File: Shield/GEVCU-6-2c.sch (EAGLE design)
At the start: 242 parts, among them IC10 ISO1050DW, IC9 ISO1050DW, U1 ATSAM3X8EA-AU, U11 ADE7913, U12 ADE7913, U24 ADE7913, U3 ADUM3221BRZ, U4 ADUM3221BRZ, U5 ADUM3221BRZ, U6 ADUM3221BRZ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

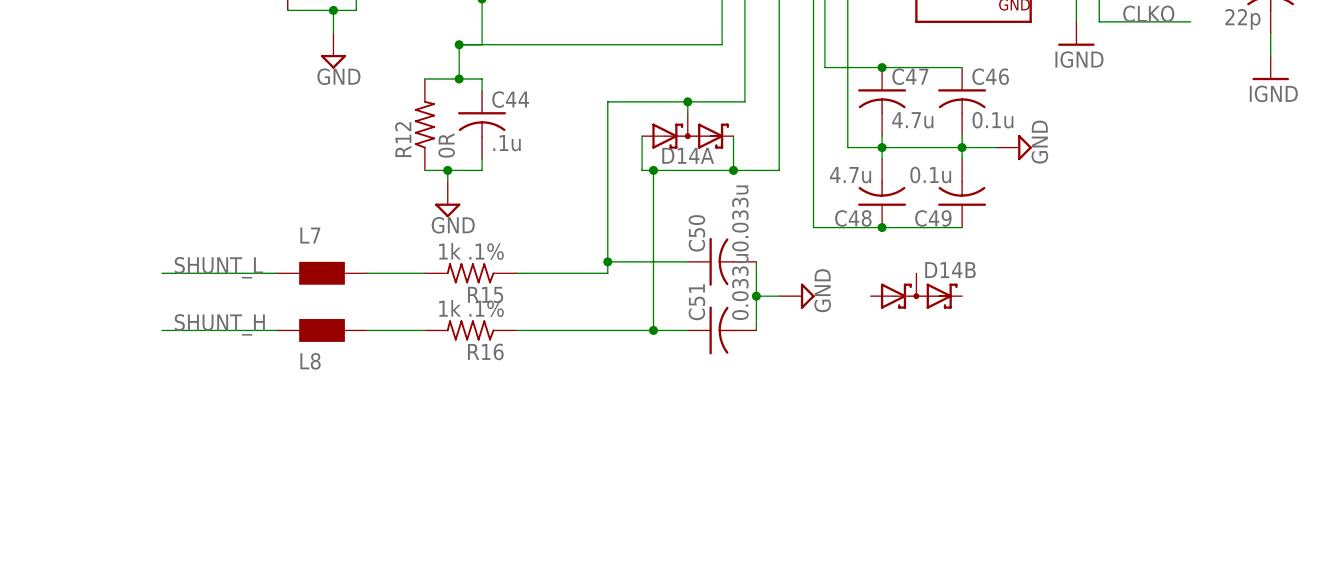
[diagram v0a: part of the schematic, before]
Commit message: Fixes on GEVCU board files, addition of an Eagle library that contains some of the parts on the GEVCU board.
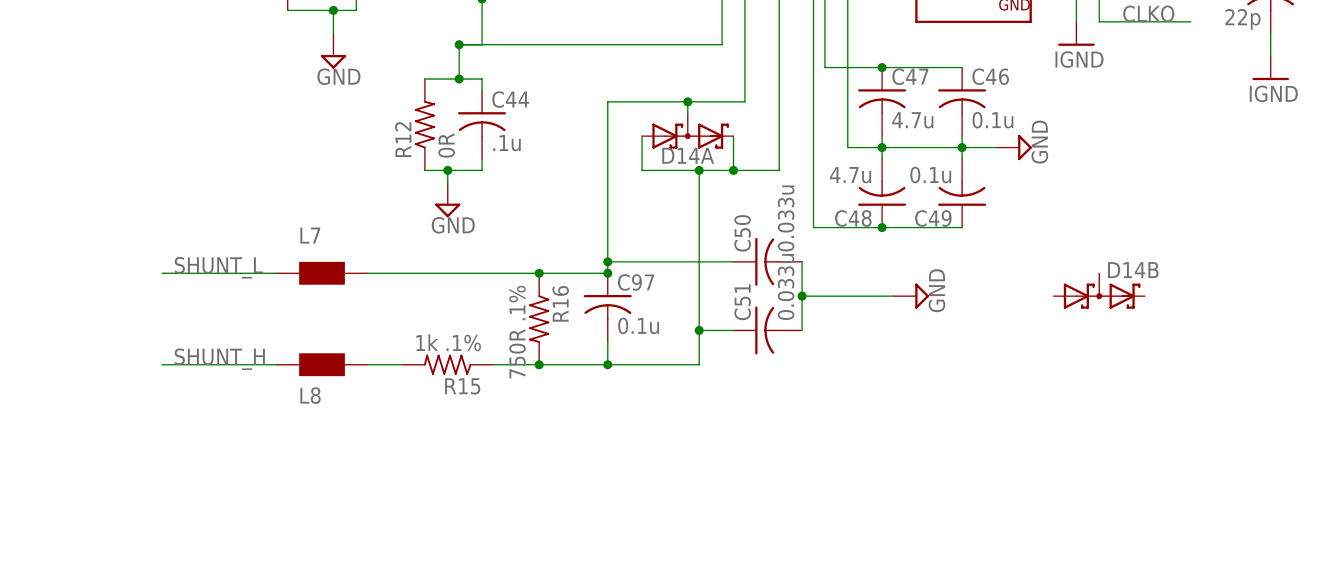
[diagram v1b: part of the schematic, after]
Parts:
- added C97: 0.1u, rcl:C-USC0805
- R16: value 1k .1% -> 750R .1%
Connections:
- removed net N$20: C50.1, D14A.C1A2, R15.1, U11.P$6
- removed net N$25: L8.1, R16.2
- new net N$7: L8.1, R15.2
- net N$21: now also C97.2, R15.1, R16.2; no longer R16.1
- net N$22: now also C50.1, C97.1, D14A.C1A2, R16.1, U11.P$6; no longer R15.2
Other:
- moved on the sheet: C50, C51, D14B, L8, R15, R16
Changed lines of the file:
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@@
 <?xml version="1.0" encoding="utf-8"?>
 <!DOCTYPE eagle SYSTEM "eagle.dtd">
-<eagle version="6.5.0">
+<eagle version="6.6.0">
 <drawing>
 <settings>
@@
 <part name="L8" library="wuerth-elektronik" deviceset="WE-CBF" device="_0805" value="MH2029-300Y"/>
 <part name="R15" library="rcl" deviceset="R-US_" device="R0805" value="1k .1%"/>
-<part name="R16" library="rcl" deviceset="R-US_" device="R0805" value="1k .1%"/>
+<part name="R16" library="rcl" deviceset="R-US_" device="R0805" value="750R .1%"/>
 <part name="C50" library="rcl" deviceset="C-US" device="C0805" value="0.033u"/>
 <part name="C51" library="rcl" deviceset="C-US" device="C0805" value="0.033u"/>
@@
 <part name="C85" library="rcl" deviceset="C-US" device="C0805" value="10u"/>
 <part name="U$4" library="collin" deviceset="BLE_SPI" device=""/>
+<part name="C97" library="rcl" deviceset="C-US" device="C0805" value="0.1u"/>
 </parts>
 <sheets>
@@
 <attribute name="NAME" x="490.22" y="393.7" size="1.778" layer="95" rot="R180"/>
 </instance>
-<instance part="L8" gate="G$1" x="490.22" y="384.81" smashed="yes" rot="R180">
-<attribute name="NAME" x="490.22" y="379.73" size="1.778" layer="95" rot="R180"/>
+<instance part="L8" gate="G$1" x="490.22" y="381" smashed="yes" rot="R180">
+<attribute name="NAME" x="490.22" y="375.92" size="1.778" layer="95" rot="R180"/>
 </instance>
-<instance part="R15" gate="G$1" x="506.73" y="388.62" rot="R180"/>
-<instance part="R16" gate="G$1" x="506.73" y="382.27" rot="R180"/>
-<instance part="C50" gate="G$1" x="533.4" y="389.89" rot="R90"/>
-<instance part="C51" gate="G$1" x="533.4" y="382.27" rot="R90"/>
-<instance part="0V16" gate="GND" x="543.56" y="386.08" rot="R90"/>
+<instance part="R15" gate="G$1" x="504.19" y="378.46" rot="R180"/>
+<instance part="R16" gate="G$1" x="514.35" y="383.54" rot="R270"/>
+<instance part="C50" gate="G$1" x="538.48" y="389.89" rot="R90"/>
+<instance part="C51" gate="G$1" x="538.48" y="382.27" rot="R90"/>
+<instance part="0V16" gate="GND" x="556.26" y="386.08" rot="R90"/>
 <instance part="C52" gate="G$1" x="584.2" y="444.5" rot="R270"/>
 <instance part="C53" gate="G$1" x="584.2" y="450.85" rot="MR90"/>
@@
 <attribute name="NAME" x="527.812" y="400.7866" size="1.778" layer="95"/>
 </instance>
-<instance part="D14" gate="B" x="556.26" y="386.08" smashed="yes">
-<attribute name="NAME" x="557.022" y="388.0866" size="1.778" layer="95"/>
+<instance part="D14" gate="B" x="576.58" y="386.08" smashed="yes">
+<attribute name="NAME" x="577.342" y="388.0866" size="1.778" layer="95"/>
 </instance>
 <instance part="U$3" gate="G$1" x="612.14" y="424.18" rot="R180"/>
@@
 <instance part="C85" gate="G$1" x="490.22" y="257.81"/>
 <instance part="U$4" gate="G$1" x="513.08" y="259.08"/>
+<instance part="C97" gate="G$1" x="521.97" y="386.08"/>
 </instances>
 <busses>
@@
 <pinref part="C50" gate="G$1" pin="2"/>
 <pinref part="C51" gate="G$1" pin="2"/>
-<wire x1="538.48" y1="389.89" x2="538.48" y2="386.08" width="0.1524" layer="91"/>
+<wire x1="543.56" y1="389.89" x2="543.56" y2="386.08" width="0.1524" layer="91"/>
 <pinref part="0V16" gate="GND" pin="GND"/>
-<wire x1="538.48" y1="386.08" x2="538.48" y2="382.27" width="0.1524" layer="91"/>
-<wire x1="541.02" y1="386.08" x2="538.48" y2="386.08" width="0.1524" layer="91"/>
-<junction x="538.48" y="386.08"/>
+<wire x1="543.56" y1="386.08" x2="543.56" y2="382.27" width="0.1524" layer="91"/>
+<wire x1="553.72" y1="386.08" x2="543.56" y2="386.08" width="0.1524" layer="91"/>
+<junction x="543.56" y="386.08"/>
 </segment>
 <segment>
@@
 </segment>
 </net>
-<net name="N$20" class="0">
-<segment>
-<pinref part="U11" gate="G$1" pin="P$6"/>
-<wire x1="551.18" y1="429.26" x2="537.21" y2="429.26" width="0.1524" layer="91"/>
-<wire x1="537.21" y1="429.26" x2="537.21" y2="407.67" width="0.1524" layer="91"/>
-<wire x1="537.21" y1="407.67" x2="530.86" y2="407.67" width="0.1524" layer="91"/>
-<pinref part="R15" gate="G$1" pin="1"/>
-<wire x1="530.86" y1="407.67" x2="521.97" y2="407.67" width="0.1524" layer="91"/>
-<wire x1="511.81" y1="388.62" x2="521.97" y2="388.62" width="0.1524" layer="91"/>
-<wire x1="521.97" y1="388.62" x2="521.97" y2="389.89" width="0.1524" layer="91"/>
-<wire x1="521.97" y1="389.89" x2="521.97" y2="407.67" width="0.1524" layer="91"/>
-<pinref part="C50" gate="G$1" pin="1"/>
-<wire x1="530.86" y1="389.89" x2="521.97" y2="389.89" width="0.1524" layer="91"/>
-<junction x="521.97" y="389.89"/>
-<pinref part="D14" gate="A" pin="C1A2"/>
-<wire x1="530.86" y1="406.4" x2="530.86" y2="407.67" width="0.1524" layer="91"/>
-<junction x="530.86" y="407.67"/>
-</segment>
-</net>
 <net name="N$21" class="0">
 <segment>
-<wire x1="527.05" y1="400.05" x2="535.94" y2="400.05" width="0.1524" layer="91"/>
+<wire x1="532.13" y1="400.05" x2="535.94" y2="400.05" width="0.1524" layer="91"/>
 <wire x1="535.94" y1="400.05" x2="541.02" y2="400.05" width="0.1524" layer="91"/>
 <wire x1="541.02" y1="400.05" x2="541.02" y2="426.72" width="0.1524" layer="91"/>
 <pinref part="U11" gate="G$1" pin="P$7"/>
 <wire x1="541.02" y1="426.72" x2="551.18" y2="426.72" width="0.1524" layer="91"/>
-<pinref part="R16" gate="G$1" pin="1"/>
-<wire x1="511.81" y1="382.27" x2="527.05" y2="382.27" width="0.1524" layer="91"/>
-<wire x1="527.05" y1="382.27" x2="527.05" y2="400.05" width="0.1524" layer="91"/>
+<wire x1="532.13" y1="382.27" x2="532.13" y2="400.05" width="0.1524" layer="91"/>
 <pinref part="C51" gate="G$1" pin="1"/>
-<wire x1="530.86" y1="382.27" x2="527.05" y2="382.27" width="0.1524" layer="91"/>
-<junction x="527.05" y="382.27"/>
+<wire x1="535.94" y1="382.27" x2="532.13" y2="382.27" width="0.1524" layer="91"/>
 <pinref part="D14" gate="A" pin="A1"/>
 <wire x1="525.78" y1="403.86" x2="525.78" y2="400.05" width="0.1524" layer="91"/>
-<wire x1="525.78" y1="400.05" x2="527.05" y2="400.05" width="0.1524" layer="91"/>
-<junction x="527.05" y="400.05"/>
+<wire x1="525.78" y1="400.05" x2="532.13" y2="400.05" width="0.1524" layer="91"/>
+<junction x="532.13" y="400.05"/>
 <pinref part="D14" gate="A" pin="C2"/>
 <wire x1="535.94" y1="403.86" x2="535.94" y2="400.05" width="0.1524" layer="91"/>
 <junction x="535.94" y="400.05"/>
-</segment>
-</net>
-<net name="N$22" class="0">
-<segment>
-<pinref part="L7" gate="G$1" pin="1"/>
-<pinref part="R15" gate="G$1" pin="2"/>
-<wire x1="495.3" y1="388.62" x2="501.65" y2="388.62" width="0.1524" layer="91"/>
-</segment>
-</net>
-<net name="N$25" class="0">
-<segment>
-<pinref part="L8" gate="G$1" pin="1"/>
 <pinref part="R16" gate="G$1" pin="2"/>
-<wire x1="495.3" y1="382.27" x2="501.65" y2="382.27" width="0.1524" layer="91"/>
+<pinref part="C97" gate="G$1" pin="2"/>
+<wire x1="514.35" y1="378.46" x2="521.97" y2="378.46" width="0.1524" layer="91"/>
+<wire x1="521.97" y1="378.46" x2="521.97" y2="381" width="0.1524" layer="91"/>
+<wire x1="532.13" y1="382.27" x2="532.13" y2="378.46" width="0.1524" layer="91"/>
+<wire x1="532.13" y1="378.46" x2="521.97" y2="378.46" width="0.1524" layer="91"/>
+<junction x="532.13" y="382.27"/>
+<junction x="521.97" y="378.46"/>
+<pinref part="R15" gate="G$1" pin="1"/>
+<wire x1="514.35" y1="378.46" x2="509.27" y2="378.46" width="0.1524" layer="91"/>
+<junction x="514.35" y="378.46"/>
 </segment>
 </net>
@@
 <segment>
 <pinref part="L8" gate="G$1" pin="2"/>
-<wire x1="485.14" y1="382.27" x2="472.44" y2="382.27" width="0.1524" layer="91"/>
-<label x="473.71" y="382.27" size="1.778" layer="95"/>
+<wire x1="485.14" y1="378.46" x2="472.44" y2="378.46" width="0.1524" layer="91"/>
+<label x="473.71" y="378.46" size="1.778" layer="95"/>
 </segment>
 </net>
@@
 </segment>
 </net>
+<net name="N$22" class="0">
+<segment>
+<pinref part="R16" gate="G$1" pin="1"/>
+<pinref part="C97" gate="G$1" pin="1"/>
+<wire x1="514.35" y1="388.62" x2="521.97" y2="388.62" width="0.1524" layer="91"/>
+<pinref part="U11" gate="G$1" pin="P$6"/>
+<wire x1="551.18" y1="429.26" x2="537.21" y2="429.26" width="0.1524" layer="91"/>
+<wire x1="537.21" y1="429.26" x2="537.21" y2="407.67" width="0.1524" layer="91"/>
+<wire x1="537.21" y1="407.67" x2="530.86" y2="407.67" width="0.1524" layer="91"/>
+<wire x1="530.86" y1="407.67" x2="521.97" y2="407.67" width="0.1524" layer="91"/>
+<wire x1="521.97" y1="389.89" x2="521.97" y2="407.67" width="0.1524" layer="91"/>
+<pinref part="C50" gate="G$1" pin="1"/>
+<wire x1="535.94" y1="389.89" x2="521.97" y2="389.89" width="0.1524" layer="91"/>
+<pinref part="D14" gate="A" pin="C1A2"/>
+<wire x1="530.86" y1="406.4" x2="530.86" y2="407.67" width="0.1524" layer="91"/>
+<junction x="530.86" y="407.67"/>
+<wire x1="521.97" y1="388.62" x2="521.97" y2="389.89" width="0.1524" layer="91"/>
+<junction x="521.97" y="388.62"/>
+<junction x="521.97" y="389.89"/>
+<pinref part="L7" gate="G$1" pin="1"/>
+<wire x1="514.35" y1="388.62" x2="495.3" y2="388.62" width="0.1524" layer="91"/>
+<junction x="514.35" y="388.62"/>
+</segment>
+</net>
+<net name="N$7" class="0">
+<segment>
+<pinref part="R15" gate="G$1" pin="2"/>
+<pinref part="L8" gate="G$1" pin="1"/>
+<wire x1="499.11" y1="378.46" x2="495.3" y2="378.46" width="0.1524" layer="91"/>
+</segment>
+</net>
